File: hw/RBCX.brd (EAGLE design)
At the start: 100 x 100 mm, 470 parts, among them IC1 AMS1117-3.3, IC10 INA180A4, IC11 INA180A4, IC12 MPU-6050, IC13 STM32F103VCT6, IC2 DRV8833PWP, IC3 INA180A4, IC4 INA180A4, IC5 DRV8833PWP, IC6 INA180A4, IC7 INA180A4, IC8 INA180A4, IC9 INA180A4, P1 M1, P2 M2, P3 M3, P4 M4, Q1 NCE20P45Q, Q10 2N7002, Q2 NCE20P45Q, Q3 2N7002, Q4 2N7002, Q5 2N7002, Q6 2N7002, Q7 2N7002, Q8 2N7002, Q9 2N7002, X1 POWER_IN, X2 POWER_OUT, X3 52559-3092, X4 uUSB, Y1 5032/2P, Y2 3215_2P

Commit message: hw: jumpers modified to match 0603 resistors
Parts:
- removed R119, R126, R24, R25, R26, R47, R58: 0R, rcl_upravena:R0603
- SJ1, SJ2, SJ3, SJ4, SJ5, SJ8, SJ9: device jumper:SJ_2 -> jumper:SJ_2_DEFAULT
- SJ6, SJ7: device jumper:SJ_2 -> jumper:SJ_2_0603
- turned SJ1 to 270 degrees
- turned SJ2 to 270 degrees
- turned SJ4 to 0 degrees
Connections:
- net +3V3: now also SJ1.3, SJ2.3; no longer R26.1, R58.1, SJ1.1, SJ2.1
- net +3V3S: now also SJ4.3; no longer R119.1, R126.1, SJ4.1
- net +5V: now also SJ1.1, SJ2.1, SJ4.1; no longer R24.2, R25.2, R47.2, SJ1.3, SJ2.3, SJ4.3
- net ENC12_PWR: no longer R119.2
- net ENC34_PWR: no longer R126.2
- net ESP-I2C-PWR: no longer R25.1
- net ESP_SPI_PWR: no longer R24.1
- net ESP_UCOM_PWR: no longer R58.2
- net ESP_USART_PWR: no longer R26.2
- net STM_UART_PWR: no longer R47.1
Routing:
- net +5V: track 77.6 -> 71.2 mm

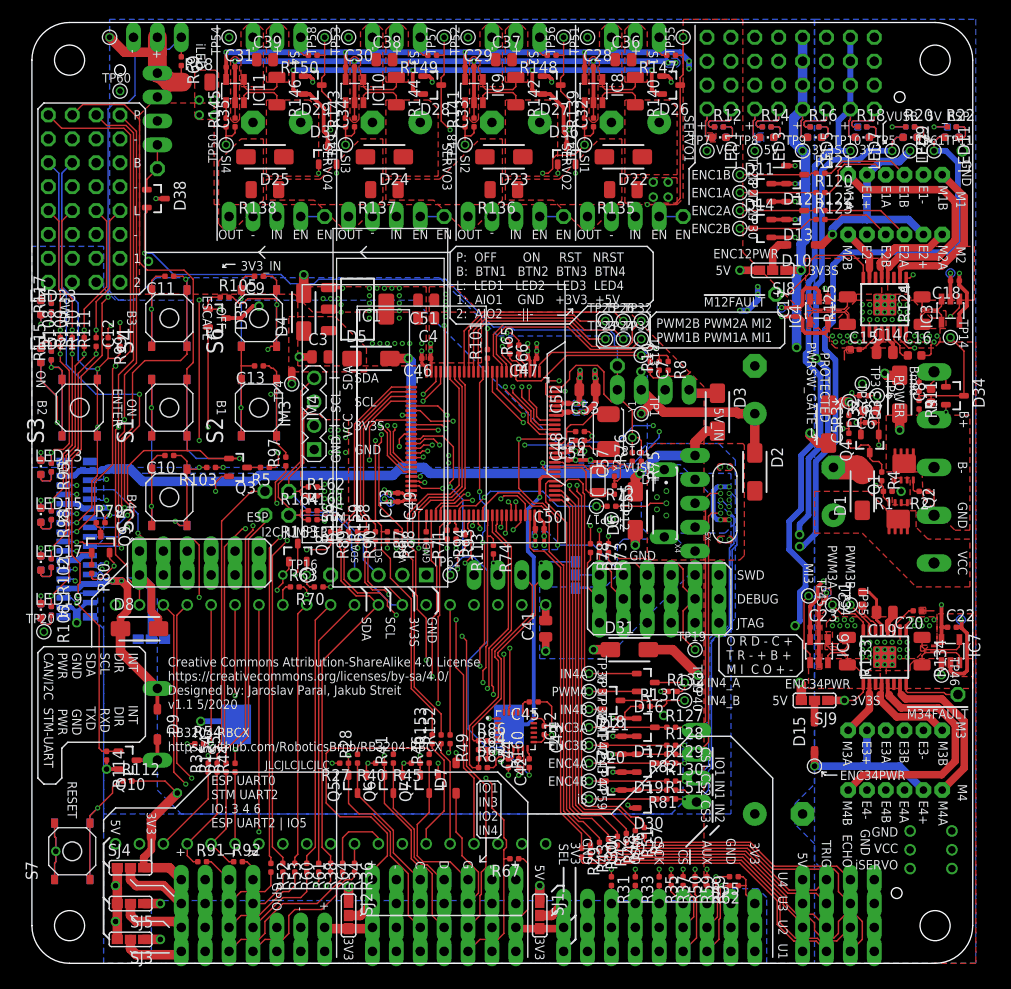
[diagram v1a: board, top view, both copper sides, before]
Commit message: hw: renumber parts
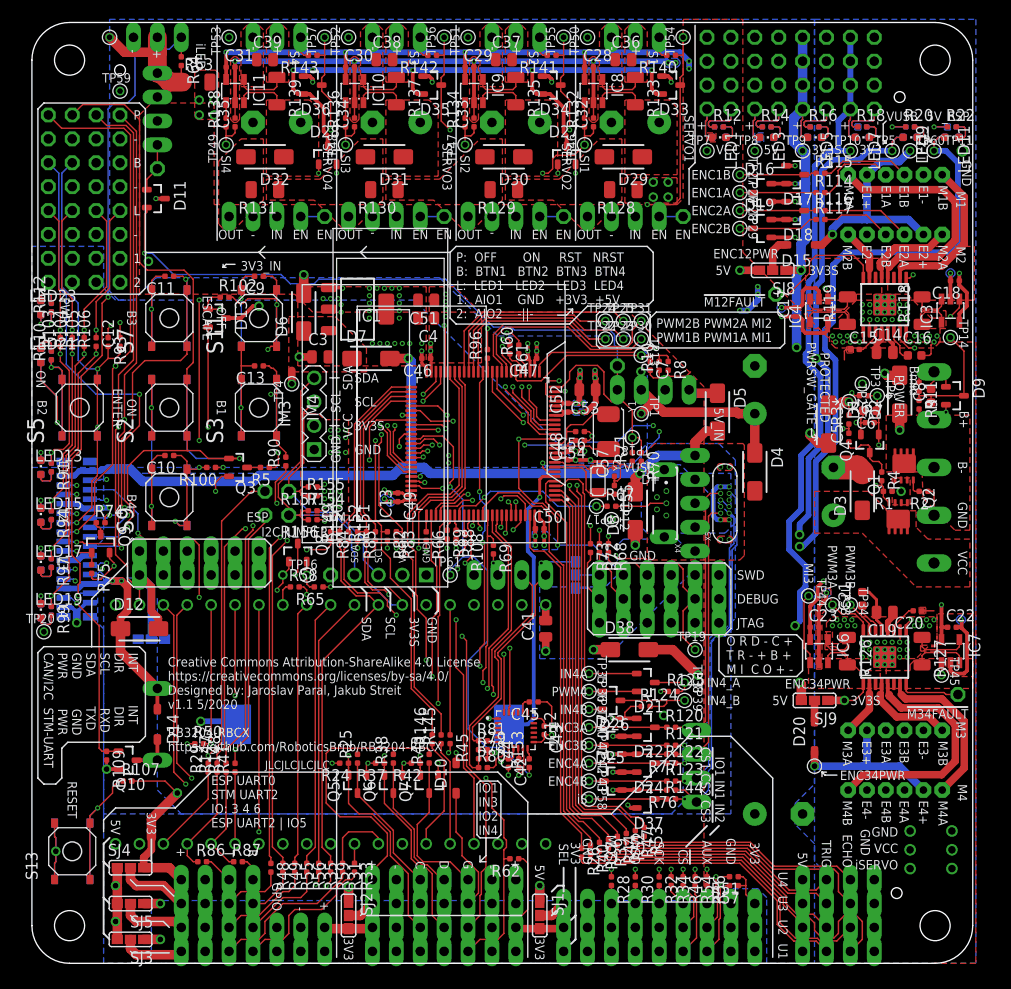
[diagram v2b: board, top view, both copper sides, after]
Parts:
- removed R158, R159, R160, R163, R164: 330R, rcl_upravena:R0402
- removed R161, R162: 4k7, rcl_upravena:R0402
- removed TP62: (no value), test_points:TP_06
- added R119, R126: 5m, rcl_upravena:R1206
- added R24, R25: 4k7, rcl_upravena:R0402
- added R26, R47, R58: 330R, rcl_upravena:R0402
- added TP21: (no value), test_points:TP_06
- D11, D13, D26, D27, D28: value BAS40-04 -> BAS40-05
- D12, D29, D30: value BAS40-04 -> SS34; device diode:SOT23 -> diode:SMA
- D14, D20: value BAS40-04 -> B5819W; device diode:SOT23 -> diode:SOD123
- D16, D35, D36, D37: value BAS40-05 -> BAS40-04
- D22, D23, D24, D25, D33: value SS34 -> BAS40-04; device diode:SMA -> diode:SOT23
- D38: value BAS40-05 -> SS34; device diode:SOT23 -> diode:SMA
- D7: value B5819W -> SS34; device diode:SOD123 -> diode:SMA
- D9: value B5819W -> BAS40-04; device diode:SOD123 -> diode:SOT23
- JP10: value ESP_UART -> ESP_I2C_AUX1_VSEL; device pinhead:1X04 -> pinhead:1X03
- JP11: value ESP_I2C_AUX1_VSEL -> ESP_UART_AUX
- JP12: value ESP_UART_AUX -> ESP_SPI_AUX1
- JP13: value ESP_SPI_AUX1 -> UTS2; device pinhead:1X03 -> pinhead:1X04
- JP14: value UTS2 -> ESP_I2C2_VSEL
- JP15: value ESP_I2C2_VSEL -> ESP_SPI2; device pinhead:1X04 -> pinhead:1X06
- JP16: value ESP_SPI2 -> UTS3; device pinhead:1X06 -> pinhead:1X04
- JP17: value UTS3 -> ESP_I2C_AUX2_VSEL; device pinhead:1X04 -> pinhead:1X03
- JP18: value ESP_I2C_AUX2_VSEL -> STM_UART; device pinhead:1X03 -> pinhead:1X04
- JP19: value STM_UART -> ESP_SPI_AUX2; device pinhead:1X04 -> pinhead:1X03
- JP20: value ESP_SPI_AUX2 -> UTS4; device pinhead:1X03 -> pinhead:1X04
- JP21: value UTS4 -> ESP_SPI3; device pinhead:1X04 -> pinhead:1X06
- JP22: value ESP_SPI3 -> ESP_I2C1; device pinhead:1X06 -> pinhead:1X04
- JP23: value ESP_I2C1 -> ESP_UCOM
- JP24: value ESP_UCOM -> ESP_SPI_AUX3; device pinhead:1X04 -> pinhead:1X03
- JP25: value ESP_SPI_AUX3 -> ESP_I2C_AUX1
- JP26: value ESP_I2C_AUX1 -> ESP_UCOM_AUX
- JP27: value ESP_UCOM_AUX -> ILED_EN; device pinhead:1X03 -> pinhead:1X01
- JP29: value ILED_EN -> AIO; device pinhead:1X01 -> pinhead:2X04
- JP30: value AIO -> ESP_I2C_AUX2; device pinhead:2X04 -> pinhead:1X03
- JP31: value ESP_I2C_AUX2 -> ILED
- JP32: value ILED -> USB; device pinhead:1X03 -> pinhead:1X05
- JP33: value USB -> SWD; device pinhead:1X05 -> pinhead:1X06
- JP34: value SWD -> DEBUG; device pinhead:1X06 -> pinhead:1X04
- JP35: value DEBUG -> USBC_AUX
- JP4: value BUZZER -> +5V; device pinhead:1X01 -> pinhead:2X04
- JP42: value BUTTONS -> LEDS
- JP43: value LEDS -> BUTTONS
- JP44: value PWR_BUTTONS -> BUZZER; device pinhead:2X04 -> pinhead:1X01
- JP45: value M12FAULT -> PWR_BUTTONS; device pinhead:1X01 -> pinhead:2X04
- JP46: value M34FAULT -> M12FAULT
- JP47: value SERVO1_EN -> M34FAULT
- JP48: value SERVO2_EN -> SERVO1_EN
- JP49: value SERVO3_EN -> SERVO2_EN
- JP5: value +5V -> VCC
- JP50: value SERVO4_EN -> SERVO3_EN
- JP51: value SERVO1 -> SERVO4_EN; device pinhead:1X03 -> pinhead:1X01
- JP52: value SERVO2 -> SERVO1
- JP53: value SERVO3 -> SERVO2
- JP54: value SERVO4 -> SERVO3
- JP55: value INTELIGENT_SERVO1 -> SERVO4; device iServo_connector:292161-3 -> pinhead:1X03
- JP56: value INTELIGENT_SERVO2 -> INTELIGENT_SERVO1
- JP57: value I2C_INTERCONNECT -> INTELIGENT_SERVO2; device pinhead:2X02 -> iServo_connector:292161-3
- JP58: value USBC_AUX -> I2C_INTERCONNECT; device pinhead:1X04 -> pinhead:2X02
- JP6: value VCC -> UTS1; device pinhead:2X04 -> pinhead:1X04
- JP7: value UTS1 -> ESP_I2C1_VSEL
- JP8: value ESP_I2C1_VSEL -> ESP_SPI1; device pinhead:1X04 -> pinhead:1X06
- JP9: value ESP_SPI1 -> ESP_UART; device pinhead:1X06 -> pinhead:1X04
- R102: value 330R -> 2k2
- R105, R147, R148, R149, R150, R151: value 2k2 -> 330R
- R107, R109: value 330R -> 1M
- R110, R111, R154, R155, R37, R38, R42, R43, R50, R64, R78: value 330R -> 4k7
- R112: value 1M -> 1k
- R113, R77: value 330R -> 1k
- R114: value 1M -> 2k2
- R115, R116: value 4k7 -> 2k2
- R117, R141, R143: value 1k -> 2k2
- R118, R139: value 1k -> 5m; device rcl_upravena:R0402 -> rcl_upravena:R1206
- R124, R125: value 5m -> 10k; device rcl_upravena:R1206 -> rcl_upravena:R0402
- R127: value 2k2 -> 5m; device rcl_upravena:R0402 -> rcl_upravena:R1206
- R128, R129, R130: value 2k2 -> 0R; device rcl_upravena:R0402 -> rcl_upravena:R1206
- R131: value 10k -> 0R; device rcl_upravena:R0402 -> rcl_upravena:R1206
- R132, R76: value 10k -> 1k
- R134: value 5m -> 1k; device rcl_upravena:R1206 -> rcl_upravena:R0402
- R135, R137: value 0R -> 5m
- R136, R138: value 0R -> 1k; device rcl_upravena:R1206 -> rcl_upravena:R0402
- R140, R142, R144: value 5m -> 2k2; device rcl_upravena:R1206 -> rcl_upravena:R0402
- R145, R81, R82: value 1k -> 330R
- R146: value 5m -> 330R; device rcl_upravena:R1206 -> rcl_upravena:R0402
- R27, R28, R40, R41, R45, R46, R54, R69, R83, R84: value 4k7 -> 330R
- R51, R57, R74: value 330R -> 100k
- R55, R80: value 100k -> 330R
- R62, R79: value 100k -> 4k7
- R63: value 330R -> 0R; device rcl_upravena:R0402 -> rcl_upravena:R1206
- R67: value 4k7 -> 1k5
- R68: value 0R -> 330R; device rcl_upravena:R1206 -> rcl_upravena:R0402
- R70: value 330R -> 5k6
- R71: value 330R -> 10k
- R72: value 1k5 -> 330R
- R75: value 5k6 -> 100k
- moved JP55 109.5 mm to (26.0, 98.4), turned to 0 degrees
- moved JP31 103.5 mm to (13.3, 98.4), turned to 0 degrees
- moved R114 96.6 mm to (83.8, 81.9), turned to 0 degrees
- moved JP6 94.2 mm to (85.7, 1.27), turned to 180 degrees
- moved R118 92.6 mm to (94.6, 69.4), flipped to the top
- moved D9 91.7 mm to (98.1, 60.3), turned to 180 degrees
- moved TP59 90.3 mm to (9.37, 92.7), turned to 0 degrees
- moved R147 89.8 mm to (19.7, 20.8), turned to 90 degrees
- moved R64 87.2 mm to (15.9, 95.9)
- moved TP60 86.8 mm to (95.9, 86.4)
- moved TP58 85.7 mm to (59.2, 17.5), turned to 270 degrees
- moved D12 84.8 mm to (11.4, 35.6), turned to 0 degrees
- moved JP30 84.4 mm to (48.9, 1.27)
- moved R115 84.0 mm to (83.8, 84.0), turned to 0 degrees
- moved R148 83.3 mm to (20.6, 20.8), turned to 90 degrees
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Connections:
- net !M12_FAULT: now also JP46.1; no longer JP45.1
- net !M34_FAULT: now also JP47.1; no longer JP46.1
- net +3V3: now also JP11.3, JP15.1, JP19.3, JP21.1, JP24.3, JP30.3, R24.2, R37.2, R42.2, R50.1, R51.1, R57.1; no longer JP13.3, JP16.1, JP20.3, JP23.1, JP27.3, JP31.3, R27.2, R40.2, R45.2, R54.1, R55.1, R67.1
- net +3V3S: now also D11.3, D13.3, D16.2, D22.2, D23.2, D24.2, D25.2, D27.3, D28.3, D33.2, D35.2, D36.2, D37.2, D9.2, JP29.5, JP29.6, JP33.1, R107.2, R154.2, R155.2, R78.2, R79.2; no longer D11.2, D12.2, D13.2, D14.2, D20.2, D26.2, D27.2, D28.2, D29.2, D30.2, D35.3, D36.3, D37.3, D38.3, JP30.5, JP30.6, JP35.1, R112.2, R161.2, R162.2, R83.2, R84.2
- net +5V: now also D1.A, D12.C, D14.C, D38.A, D5.C, D6.A, JP13.1, JP16.1, JP20.1, JP29.7, JP29.8, JP4.1, JP4.3, JP4.5, JP4.7, JP6.1, R128.1, R63.2; no longer D3.C, D31.A, D32.A, D4.A, D8.C, D9.C, JP14.1, JP17.1, JP21.1, JP30.7, JP30.8, JP5.1, JP5.3, JP5.5, JP5.7, JP7.1, R135.1, R68.2
- net 3V3_EN: now also D11.2; no longer D38.2
- net 3V3_IN: now also D6.C, D7.C; no longer D4.C, D5.C
- net 5V_IN: now also D4.C; no longer D2.C
- net BAT+_PROTECTED: now also D1.C, D2.C; no longer D32.C, D33.C
- net BOOT0: now also R75.1; no longer R80.1
- net BOOT1_PULL-DOWN: now also R74.1; no longer R79.1
- net BUTTON-1: now also JP43.1, R90.2, S3.C, S3.D, S4.C, S4.D; no longer JP42.1, R97.2, S2.C, S2.D, S8.C, S8.D
- net BUTTON-2: now also JP43.3, R93.2, S5.C, S5.D, S6.C, S6.D; no longer JP42.3, R99.2, S3.C, S3.D, S9.C, S9.D
- net BUTTON-3: now also JP43.5, R74.2, R96.2, S7.C, S7.D, S8.C, S8.D; no longer JP42.5, R101.2, R79.2, S10.C, S10.D, S4.C, S4.D
- net BUTTON-4: now also JP43.7, R100.2, S10.C, S10.D, S9.C, S9.D; no longer JP42.7, R103.2, S11.C, S11.D, S5.C, S5.D
- net BUTTON-OFF: now also JP45.1, R102.2, S11.C, S11.D; no longer JP44.1, R105.2, S6.C, S6.D
- net BUTTON-ON: now also JP45.3, S2.C, S2.D; no longer JP44.3, S14.C, S14.D
- net BUTTON1: now also R90.1; no longer R97.1
- net BUTTON2: now also R93.1; no longer R99.1
- net BUTTON3: now also R96.1; no longer R101.1
- net BUTTON4: now also R100.1; no longer R103.1
- net BUTTON_OFF: now also D13.1, R102.1; no longer D35.1, R105.1
- net BUZZER: now also R108.1; no longer R113.1
- net BUZZER-: now also D14.A; no longer D9.A
- net BUZZER-GATE: now also JP44.1, R108.2, R109.1; no longer JP4.1, R113.2, R114.1
- net CONTROL-DIR: now also R84.2; no longer R89.2
- net CONTROL-INT: now also R85.2; no longer R90.2
- net CONTROL-RX/SDA: now also R83.2; no longer R88.2
- net CONTROL-TX/SCL: now also R82.2; no longer R87.2
- net CONTROL_RX/SDA: now also R145.2, R83.1; no longer R152.2, R88.1
- net CONTROL_TX/SCL: now also R146.2, R82.1; no longer R153.2, R87.1
- net DEBUG-RX: now also JP34.3, R72.2; no longer JP35.3, R77.2
- net DEBUG-TX: now also JP34.4, R73.2; no longer JP35.4, R78.2
- net DEBUG_RX: now also R72.1; no longer R77.1
- net DEBUG_TX: now also R73.1; no longer R78.1
- net ENC12PWR: now also D15.C, TP21.P$1; no longer D10.C, TP22.P$1
- net ENC12_PWR: now also D15.A; no longer D10.A
- net ENC1A: now also D16.3, R114.1, TP26.P$1; no longer D11.3, R120.1, TP27.P$1
- net ENC1B: now also D17.3, R115.1, TP27.P$1; no longer D12.3, R121.1, TP28.P$1
- net ENC2A: now also D18.3, R116.1, TP28.P$1; no longer D13.3, R122.1, TP29.P$1
- net ENC2B: now also D19.3, R117.1, TP29.P$1; no longer D14.3, R123.1, TP30.P$1
- net ENC34PWR: now also D20.C, TP32.P$1; no longer D15.C, TP33.P$1
- net ENC34_PWR: now also D20.A; no longer D15.A
- net ENC3A: now also D22.3, R120.1, TP40.P$1; no longer D17.3, R127.1, TP41.P$1
- net ENC3B-SWO: now also R69.2; no longer R74.2
- net ENC3B/SWO: now also D23.3, R121.1, R69.1, TP41.P$1; no longer D18.3, R128.1, R74.1, TP42.P$1
- net ENC4A: now also D24.3, R122.1, TP42.P$1; no longer D19.3, R129.1, TP43.P$1
- net ENC4B: now also D25.3, R123.1, TP43.P$1; no longer D20.3, R130.1, TP44.P$1
- net ENC_1A: now also R114.2; no longer R120.2
- net ENC_1B: now also R115.2; no longer R121.2
- net ENC_2A: now also R116.2; no longer R122.2
- net ENC_2B: now also R117.2; no longer R123.2
- net ENC_3A: now also R120.2; no longer R127.2
- net ENC_3B: now also R121.2; no longer R128.2
- net ENC_4A: now also R122.2; no longer R129.2
- net ENC_4B: now also R123.2; no longer R130.2
- net ESP-I2C-PWR: now also JP10.3, JP14.1, JP17.3, JP7.1, R25.2, R38.2, R43.2; no longer JP11.3, JP15.1, JP18.3, JP8.1, R28.2, R41.2, R46.2
- net ESP-I2C-SCL: now also JP22.3, JP58.3, R24.1, R29.2; no longer JP23.3, JP57.3, R27.1, R32.2
- net ESP-I2C-SCL-VSEL: now also JP14.3, JP7.3, R25.1; no longer JP15.3, JP8.3, R28.1
- net ESP-I2C-SDA: now also JP22.4, JP58.1, R37.1, R41.2; no longer JP23.4, JP57.1, R40.1, R44.2
- net ESP-I2C-SDA-VSEL: now also JP14.4, JP7.4, R38.1; no longer JP15.4, JP8.4, R41.1
- net ESP-SPI-!CS1: now also JP8.6, R34.2; no longer JP9.6, R37.2
- net ESP-SPI-!CS2: now also JP15.6, R46.2; no longer JP16.6, R50.2
- net ESP-SPI-!CS3: now also JP21.6, R54.2; no longer JP22.6, R59.2
- net ESP-SPI-MISO: now also JP15.4, JP21.4, JP8.4, R30.2; no longer JP16.4, JP22.4, JP9.4, R33.2
- net ESP-SPI-MOSI: now also JP15.3, JP21.3, JP8.3, R28.2; no longer JP16.3, JP22.3, JP9.3, R31.2
- net ESP-SPI-SCK: now also JP15.5, JP21.5, JP8.5, R32.2; no longer JP16.5, JP22.5, JP9.5, R35.2
- net ESP-UART-RX: now also R87.2; no longer R92.2
- net ESP-UART-TX: now also R86.2; no longer R91.2
- net ESP-USART-RX: now also JP9.3, R31.2; no longer JP10.3, R34.2
- net ESP-USART-TX: now also JP9.4, R33.2; no longer JP10.4, R36.2
- net ESP_+5V: now also D38.C, D8.C, TP60.P$1; no longer D31.C, D6.C, TP61.P$1
- net ESP_EN: now also D13.2, JP45.5, R107.1, S14.C, S14.D, TP59.P$1; no longer D35.2, JP44.5, R112.1, S7.C, S7.D, TP60.P$1
- net ESP_SPI_PWR: now also JP8.1; no longer JP9.1
- net ESP_UCOM_PWR: now also JP23.1; no longer JP24.1
- net ESP_USART_PWR: now also JP9.1; no longer JP10.1
- net EXPANDER_COM_PWR: now also D12.A; no longer D8.A
- net EXPANDER_RX: now also R146.1; no longer R153.1
- net EXPANDER_TX: now also R145.1; no longer R152.1
- net GND: now also D16.1, D22.1, D23.1, D24.1, D25.1, D3.A, D33.1, D35.1, D36.1, D37.1, D9.1, JP13.4, JP14.2, JP16.4, JP17.2, JP20.4, JP21.2, JP29.3, JP29.4, JP30.2, JP31.3, JP32.5, JP33.3, JP34.2, JP4.2, JP4.4, JP4.6, JP4.8, JP45.2, JP45.4, JP45.6, JP45.8, JP57.3, JP7.2, R109.2, R110.1, R111.1, R112.1, R113.1, R119.1, R126.1, R127.1, R71.1, R75.2, R76.2, R77.2; no longer D1.A, D11.1, D12.1, D13.1, D14.1, D20.1, D26.1, D27.1, D28.1, D29.1, D30.1, JP13.2, JP14.4, JP16.2, JP17.4, JP20.2, JP21.4, JP27.2, JP30.3, JP30.4, JP31.2, JP32.3, JP33.5, JP34.3, JP35.2, JP44.2, JP44.4, JP44.6, JP44.8, JP51.3, JP6.2, JP6.6, JP6.8, JP7.4, R114.2, R115.1, R116.1, R117.1, R131.1, R132.1, R133.1, R134.1, R76.1, R80.2, R81.2, R82.2
- net GPIO-1: now also JP12.1, R36.2; no longer JP13.1, R39.2
- net GPIO-1-VSEL: now also JP10.1, R43.1; no longer JP11.1, R46.1
- net GPIO-2: now also JP25.1, R58.2; no longer JP26.1, R63.2
- net GPIO-3: now also JP23.3, R55.2; no longer JP24.3, R60.2
- net GPIO-4: now also JP23.4, R56.2; no longer JP24.4, R61.2
- net GPIO-5: now also JP11.1, R35.2; no longer JP12.1, R38.2
- net GPIO-6: now also JP26.1, R59.2; no longer JP27.1, R64.2
- net GPIO-7: now also R42.1, R45.2; no longer R45.1, R49.2
- net GPIO1: now also R36.1; no longer R39.1
- net GPIO2: now also R58.1; no longer R63.1
- net GPIO3: now also R55.1; no longer R60.1
- net GPIO4: now also R56.1; no longer R61.1
- net GPIO5: now also R35.1; no longer R38.1
- net GPIO6/TMS: now also R149.1, R59.1; no longer R156.1, R64.1
- net GPIO7/TCK: now also R150.1, R45.1; no longer R157.1, R49.1
- net I2C_SCL: now also R29.1; no longer R32.1
- net I2C_SDA: now also R41.1; no longer R44.1
- net ILED: now also R65.2; no longer R70.2
- net ILED-5V: now also JP31.1, R64.1; no longer JP32.1, R69.1
- net ILED_EN: now also D11.1, JP27.1; no longer D38.1, JP29.1
- net ILED_PWR: now also JP31.2, R63.1, R64.2; no longer JP32.2, R68.1, R69.2
- net IN1: now also JP19.1, R51.2; no longer JP20.1, R55.2
- net IN2: now also JP24.1, R57.2; no longer JP25.1, R62.2
- net IN3: now also D10.A, R50.2; no longer D7.A, R54.2
- net IN3-5V: now also D10.C, JP17.1; no longer D7.C, JP18.1
- net IN4: now also JP30.1, R62.2; no longer JP31.1, R67.2
- net IN4A: now also D21.1, TP35.P$1; no longer D16.1, TP36.P$1
- net IN4B: now also D26.2, TP37.P$1; no longer D21.2, TP38.P$1
- net IN4_A: now also D21.3, R125.2, TP38.P$1; no longer D16.3, R132.2, TP39.P$1
- net IN4_B: now also D26.3, R124.2, TP39.P$1; no longer D21.3, R131.2, TP40.P$1
- net INTELLIGENT_SERVO: now also D37.3, R144.1, TP58.P$1; no longer D30.3, R151.1, TP59.P$1
- net ISERVO: now also JP57.1, R144.2; no longer JP55.1, R151.2
- net I_LED/TDI: now also R151.1, R65.1; no longer R158.1, R70.1
- net LED-1: now also JP42.1, R103.2; no longer JP43.1, R108.2
- net LED-2: now also JP42.3, R104.2; no longer JP43.3, R109.2
- net LED-3: now also JP42.5, R105.2; no longer JP43.5, R110.2
- net LED-4: now also JP42.7, R106.2; no longer JP43.7, R111.2
- net LED1: now also R103.1, R91.1, R92.1; no longer R108.1, R95.1, R96.1
- net LED2: now also R104.1, R94.1, R95.1; no longer R100.1, R109.1, R98.1
- net LED3: now also R105.1, R97.1, R98.1; no longer R102.1, R104.1, R110.1
- net LED4: now also R101.1, R99.1; no longer R107.1, R111.1
- net LED_1: now also R91.2; no longer R95.2
- net LED_1B: now also R92.2; no longer R96.2
- net LED_2: now also R94.2; no longer R98.2
- net LED_2B: now also R95.2; no longer R100.2
- net LED_3: now also R97.2; no longer R102.2
- net LED_3B: now also R98.2; no longer R104.2
- net LED_4: now also R99.2; no longer R106.2
- net LED_4B: now also R101.2; no longer R107.2
- net M1GND: now also R118.2; no longer R124.2
- net M2GND: now also R119.2; no longer R125.2
- net M3GND: now also R126.2; no longer R133.2
- net M4GND: now also R127.2; no longer R134.2
- net MI1: now also TP30.P$1; no longer TP31.P$1
- net MI2: now also TP31.P$1; no longer TP32.P$1
- net MI3: now also TP44.P$1; no longer TP45.P$1
- net MI4: now also TP45.P$1; no longer TP46.P$1
- net MPU-INT: now also R153.2; no longer R160.2
- net MPU-SCL: now also R78.1, R80.1; no longer R83.1, R85.1
- net MPU-SDA: now also R79.1, R81.1; no longer R84.1, R86.1
- net MPU_INT: now also R153.1, TP61.P$1; no longer R160.1, TP62.P$1
- net MPU_SCL: now also R80.2; no longer R85.2
- net MPU_SDA: now also R81.2; no longer R86.2
- net NRST: now also JP33.5, JP45.7; no longer JP34.5, JP44.7
- net PWM1A: now also TP23.P$1; no longer TP24.P$1
- net PWM1B: now also TP22.P$1; no longer TP23.P$1
- net PWM2A: now also TP25.P$1; no longer TP26.P$1
- net PWM2B: now also TP24.P$1; no longer TP25.P$1
- net PWM3A: now also TP33.P$1; no longer TP34.P$1
- net PWM3B: now also TP34.P$1; no longer TP35.P$1
- net PWM4: now also D21.2, D26.1, TP36.P$1; no longer D16.2, D21.1, TP37.P$1
- net PWRLED_+3V3S1: now also R112.2; no longer R117.2
- net PWRLED_+3V3S_B1: now also R113.2; no longer R118.2
- net PWRLED_VCC1: now also R110.2; no longer R115.2
- net PWRLED_VCC_B1: now also R111.2; no longer R116.2
- net SERVO1: now also D33.3, R140.1, TP54.P$1; no longer D26.3, R147.1, TP55.P$1
- net SERVO1PWR: now also D29.A, R128.2, R129.1; no longer D22.A, R135.2, R136.1
- net SERVO1_EN: now also D27.2, JP48.1; no longer D36.2, JP47.1
- net SERVO1_PWR: now also D29.C, R133.2; no longer D22.C, R140.2
- net SERVO2: now also D34.3, R141.1, TP55.P$1; no longer D27.3, R148.1, TP56.P$1
- net SERVO2PWR: now also D30.A, R129.2, R130.1; no longer D23.A, R136.2, R137.1
- net SERVO2_EN: now also D27.1, JP49.1; no longer D36.1, JP48.1
- net SERVO2_PWR: now also D30.C, R135.2; no longer D23.C, R142.2
- net SERVO3: now also D35.3, R142.1, TP56.P$1; no longer D28.3, R149.1, TP57.P$1
- net SERVO3PWR: now also D31.A, R130.2, R131.1; no longer D24.A, R137.2, R138.1
- net SERVO3_EN: now also D28.2, JP50.1; no longer D37.2, JP49.1
- net SERVO3_PWR: now also D31.C, R137.2; no longer D24.C, R144.2
- net SERVO4: now also D36.3, R143.1, TP57.P$1; no longer D29.3, R150.1, TP58.P$1
- net SERVO4PWR: now also D32.A, R131.2; no longer D25.A, R138.2
- net SERVO4_EN: now also D28.1, JP51.1; no longer D37.1, JP50.1
- net SERVO4_PWR: now also D32.C, R139.2; no longer D25.C, R146.2
- net SERVO_1: now also JP52.1, R140.2; no longer JP51.1, R147.2
- net SERVO_1_PWR: now also JP52.2, R133.1, TP50.P$1; no longer JP51.2, R140.1, TP51.P$1
- net SERVO_2: now also JP53.1, R141.2; no longer JP52.1, R148.2
- net SERVO_2_PWR: now also JP53.2, R135.1, TP51.P$1; no longer JP52.2, R142.1, TP52.P$1
- net SERVO_3: now also JP54.1, R142.2; no longer JP53.1, R149.2
- net SERVO_3_PWR: now also JP54.2, R137.1, TP52.P$1; no longer JP53.2, R144.1, TP53.P$1
- net SERVO_4: now also JP55.1, R143.2; no longer JP54.1, R150.2
- net SERVO_4_PWR: now also JP55.2, R139.1, TP53.P$1; no longer JP54.2, R146.1, TP54.P$1
- net SI1: now also R132.1, TP46.P$1; no longer R139.1, TP47.P$1
- net SI2: now also R134.1, TP47.P$1; no longer R141.1, TP48.P$1
- net SI3: now also R136.1, TP48.P$1; no longer R143.1, TP49.P$1
- net SI4: now also R138.1, TP49.P$1; no longer R145.1, TP50.P$1
- net SI_1: now also R132.2; no longer R139.2
- net SI_2: now also R134.2; no longer R141.2
- net SI_3: now also R136.2; no longer R143.2
- net SI_4: now also R138.2; no longer R145.2
- net SPI_!SS1: now also R34.1; no longer R37.1
- net SPI_!SS2: now also R46.1; no longer R50.1
- net SPI_!SS3!/TDO: now also R152.1, R54.1; no longer R159.1, R59.1
- net SPI_MISO: now also R30.1; no longer R33.1
- net SPI_MOSI: now also R28.1; no longer R31.1
- net SPI_SCK: now also R32.1; no longer R35.1
- net STM-AIO1: now also JP29.1, R60.2; no longer JP30.1, R65.2
- net STM-AIO2: now also JP29.2, R61.1; no longer JP30.2, R66.1
- net STM-CAN-RX: now also R89.2; no longer R94.2
- net STM-CAN-TX: now also R88.2; no longer R93.2
- net STM-I2C-SCL: now also JP58.4, R155.1, R157.2; no longer JP57.4, R162.1, R164.2
- net STM-I2C-SDA: now also JP58.2, R154.1, R156.2; no longer JP57.2, R161.1, R163.2
- net STM-UART-RX: now also JP18.4, R49.2; no longer JP19.4, R53.2
- net STM-UART-TX: now also JP18.3, R48.2; no longer JP19.3, R52.2
- net STM_AIO1: now also R60.1; no longer R65.1
- net STM_AIO2: now also R61.2; no longer R66.2
- net STM_CAN_RX: now also R89.1; no longer R94.1
- net STM_CAN_TX: now also R88.1; no longer R93.1
- net STM_I2C_SCL: now also R157.1; no longer R164.1
- net STM_I2C_SDA: now also R156.1; no longer R163.1
- net STM_SPI_!CS: now also R149.2, R84.1; no longer R156.2, R89.1
- net STM_SPI_MISO: now also R152.2, R85.1; no longer R159.2, R90.1
- net STM_SPI_MOSI: now also R151.2; no longer R158.2
- net STM_SPI_SCK: now also R150.2; no longer R157.2
- net STM_UART_PWR: now also JP18.1; no longer JP19.1
- net SWCLK: now also R66.1; no longer R71.1
- net SWCLK_: now also JP33.2, R66.2; no longer JP34.2, R71.2
- net SWDIO: now also R68.1; no longer R73.1
- net SWDIO_: now also JP33.4, R68.2; no longer JP34.4, R73.2
- net SWO: now also JP33.6; no longer JP34.6
- net TUNNEL_RX: now also R147.2; no longer R154.2
- net TUNNEL_TX: now also R148.2; no longer R155.2
- net UART2_RX: now also R31.1; no longer R34.1
- net UART2_TX: now also R33.1; no longer R36.1
- net UART_RX: now also R148.1, R87.1; no longer R155.1, R92.1
- net UART_TX: now also R147.1, R86.1; no longer R154.1, R91.1
- net USB_CC1: now also JP35.2, R77.1; no longer JP58.2, R82.1
- net USB_CC2: now also JP35.4, R76.1; no longer JP58.4, R81.1
- net USB_DM: now also JP32.2; no longer JP33.2
- net USB_DP: now also JP32.3, R67.2; no longer JP33.3, R72.2
- net USB_DP_PULLUP: now also R67.1; no longer R72.1
- net USB_ID: now also JP32.4; no longer JP33.4
- net USB_SBU1: now also JP35.1; no longer JP58.1
- net USB_SBU2: now also JP35.3; no longer JP58.3
- net USER_RX: now also R49.1; no longer R53.1
- net USER_TX: now also R48.1; no longer R52.1
- net UTS1-ECHO: now also JP6.3, R27.2; no longer JP7.3, R30.2
- net UTS1-TRIG: now also JP6.2, R26.2; no longer JP7.2, R29.2
- net UTS1_ECHO: now also R27.1; no longer R30.1
- net UTS1_TRIG: now also R26.1; no longer R29.1
- net UTS2-ECHO: now also JP13.3, R40.2; no longer JP14.3, R43.2
- net UTS2-TRIG: now also JP13.2, R39.2; no longer JP14.2, R42.2
- net UTS2_ECHO: now also R40.1; no longer R43.1
- net UTS2_TRIG: now also R39.1; no longer R42.1
- net UTS3-ECHO: now also JP16.3, R47.2; no longer JP17.3, R51.2
- net UTS3-TRIG: now also JP16.2, R44.2; no longer JP17.2, R48.2
- net UTS3_ECHO: now also R47.1; no longer R51.1
- net UTS3_TRIG: now also R44.1; no longer R48.1
- net UTS4-ECHO: now also JP20.3, R53.2; no longer JP21.3, R57.2
- net UTS4-TRIG: now also JP20.2, R52.2; no longer JP21.2, R56.2
- net UTS4_ECHO: now also R53.1; no longer R57.1
- net UTS4_TRIG: now also R52.1; no longer R56.1
- net VCC: now also D3.C, D4.A, JP5.1, JP5.3, JP5.5, JP5.7, JP57.2; no longer D1.C, D2.A, JP55.2, JP6.1, JP6.3, JP6.5, JP6.7
- net VUSB: now also D2.A, D7.A, D8.A, JP32.1, R70.2; no longer D3.A, D33.A, D6.A, JP33.1, R75.2
- net VUSB_DET: now also R70.1, R71.2; no longer R75.1, R76.2
- net V_BAT/2: now also D9.3; no longer D34.3

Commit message: hw: fix value of R74
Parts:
- R74: value 100k -> 330R
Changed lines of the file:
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@@
 <attribute name="VALUE" x="4.445" y="42.545" size="1.27" layer="27" rot="R270"/>
 </element>
-<element name="R74" library="rcl_upravena" package="R0402" value="100k" x="7.3025" y="46.83125" smashed="yes">
+<element name="R74" library="rcl_upravena" package="R0402" value="330R" x="7.3025" y="46.83125" smashed="yes">
 <attribute name="NAME" x="6.6675" y="47.46625" size="1.27" layer="25"/>
 <attribute name="VALUE" x="6.6675" y="44.92625" size="1.27" layer="27"/>

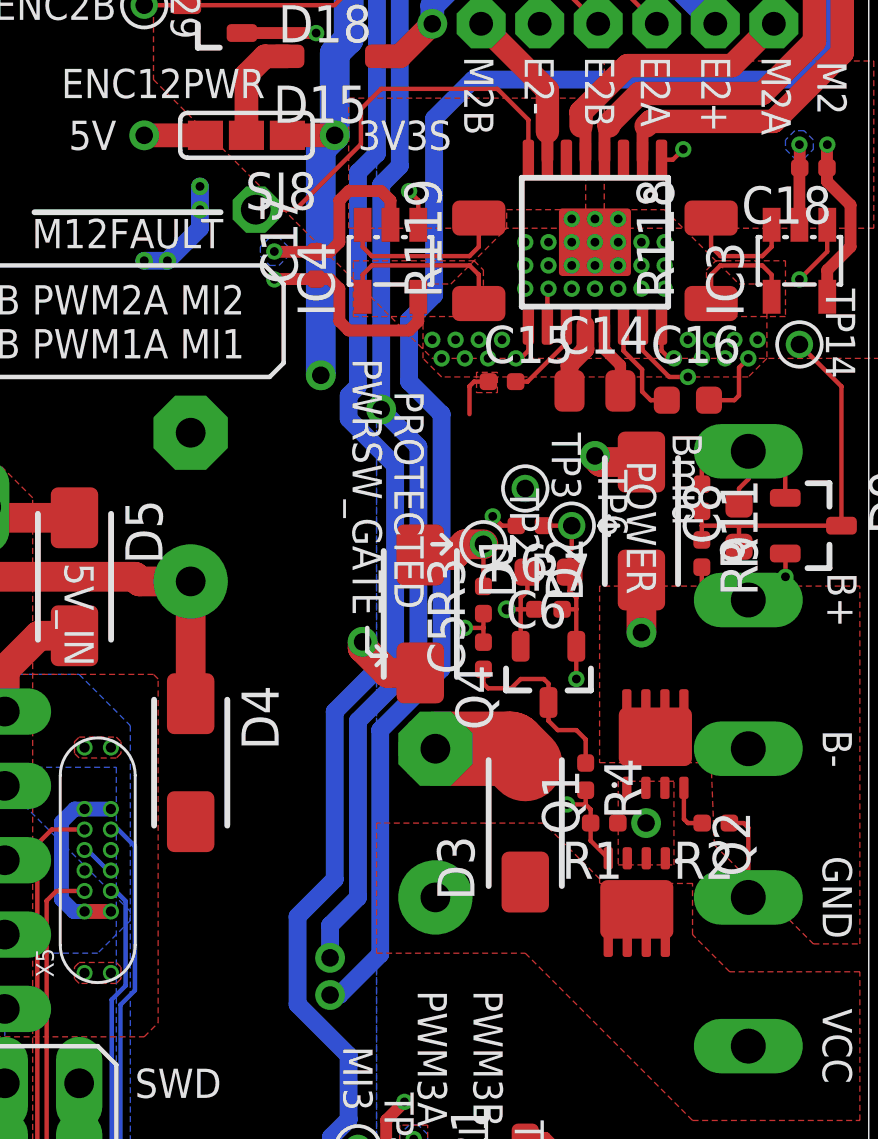
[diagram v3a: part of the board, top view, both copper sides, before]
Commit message: hw: replace D1 with smaller one (SS34 -> B5819W)
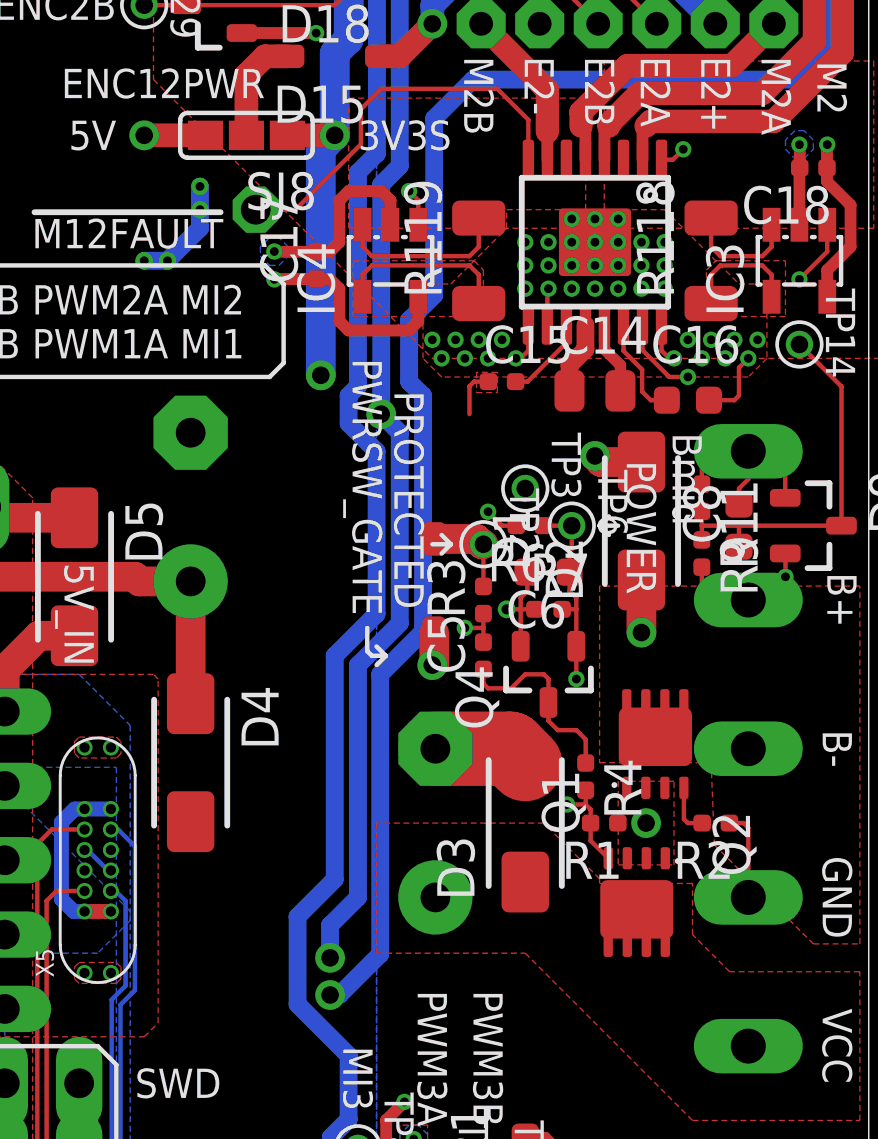
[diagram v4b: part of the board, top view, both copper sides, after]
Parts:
- D1: value SS34 -> B5819W; device diode:SMA -> diode:SOD123
- moved D1 1.06 mm to (85.2, 58.3)
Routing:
- net +5V: track 71.2 -> 87.2 mm
- net BUTTON-ON: track 156.5 -> 157.9 mm
- net POWER: track 47.1 -> 47.7 mm
- net VUSB: track 169.8 -> 169.3 mm
- net BAT+_PROTECTED: track 18.8 -> 18.2 mm
- net ESP_+5V: track 87.1 -> 86.6 mm
- net +3V3: track 122.4 -> 121.9 mm

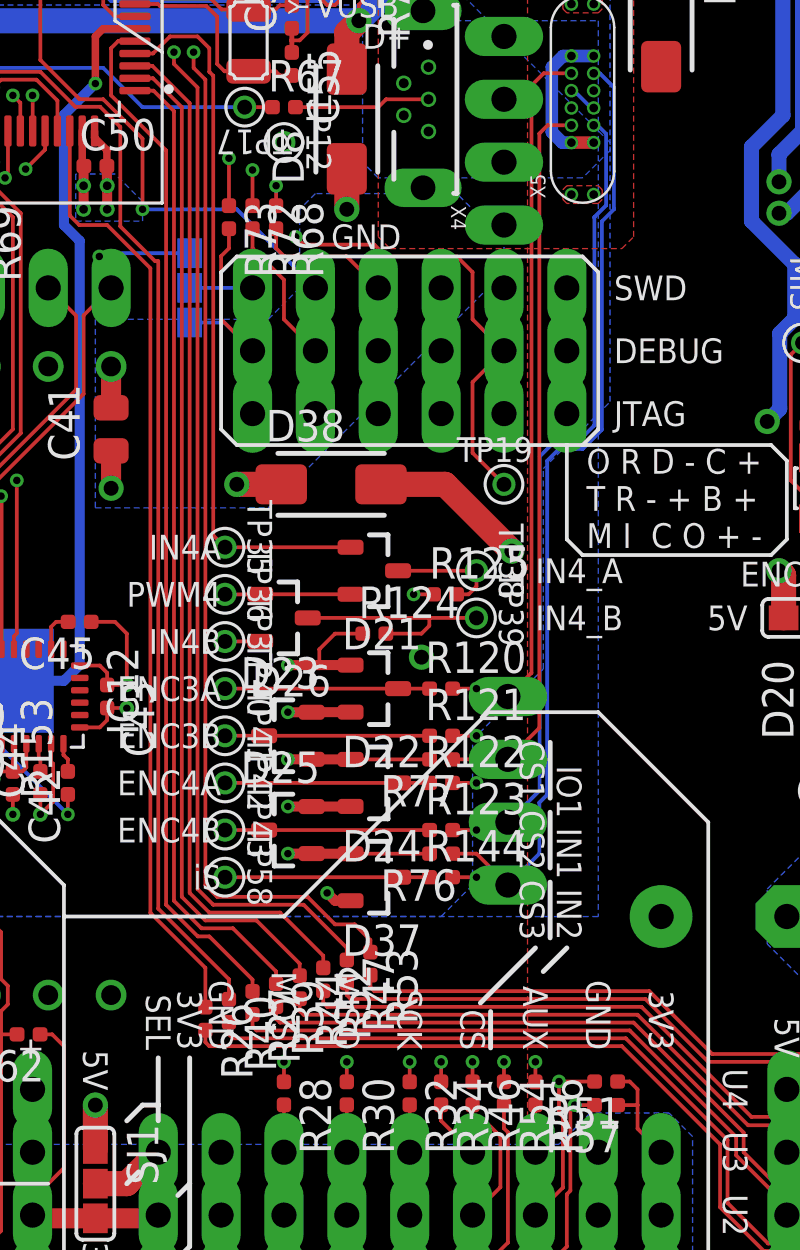
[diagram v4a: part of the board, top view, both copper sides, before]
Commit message: hw: move some resistors, because of silkscreen
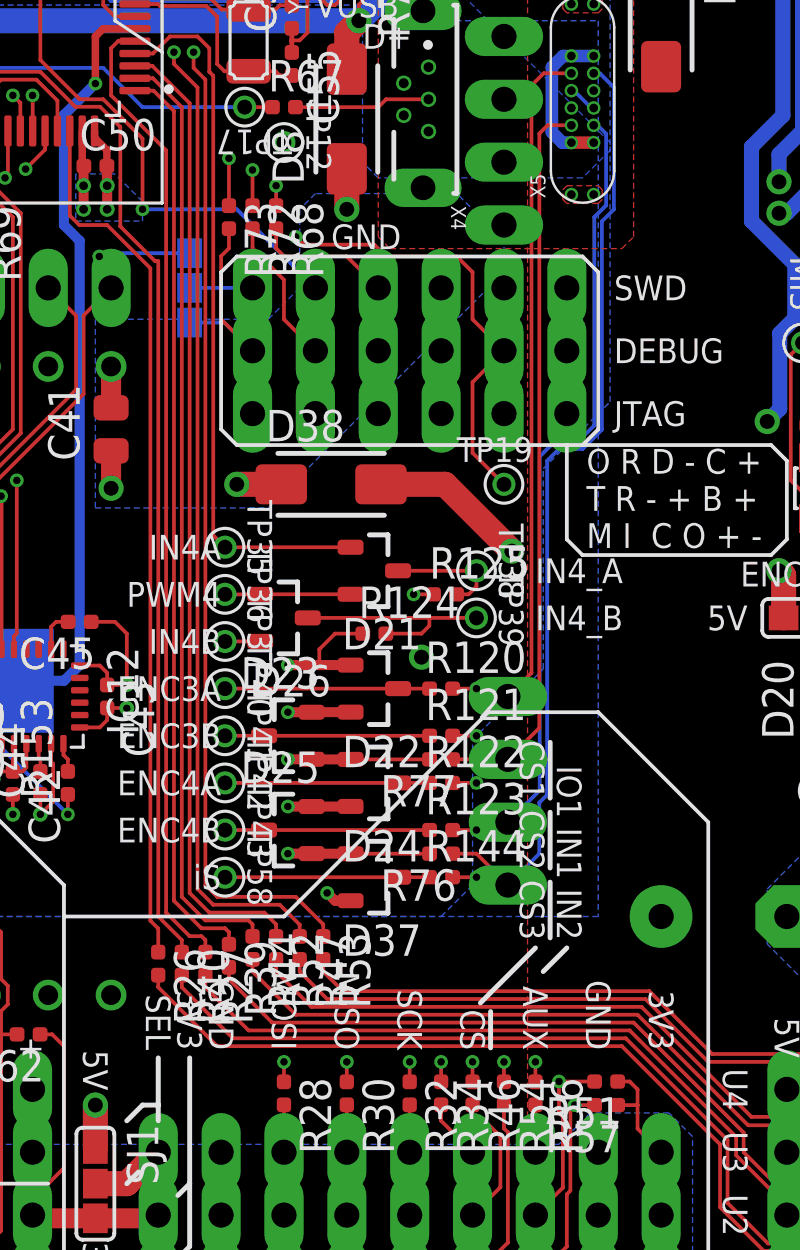
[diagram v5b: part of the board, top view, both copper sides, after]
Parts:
- moved R26 2.93 mm to (56.5, 14.0)
- moved R40 2.69 mm to (57.5, 14.0)
- moved R27 2.48 mm to (58.4, 14.0)
- moved R39 2.48 mm to (59.4, 14.3)
- moved R44 2.48 mm to (60.3, 14.6)
- moved R52 2.29 mm to (61.3, 14.6)
- moved R47 2.13 mm to (62.2, 14.6)
- moved R53 2.01 mm to (63.2, 14.6)
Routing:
- net UTS1_TRIG: track 38.3 -> 35.3 mm
- net UTS1-TRIG: track 32.0 -> 34.8 mm
- net UTS2_ECHO: track 46.6 -> 43.9 mm
- net UTS2-ECHO: track 33.8 -> 36.5 mm
- net UTS2_TRIG: track 39.6 -> 37.1 mm
- net UTS2-TRIG: track 27.4 -> 30.0 mm
- net UTS1-ECHO: track 38.6 -> 41.2 mm
- net UTS3_TRIG: track 40.7 -> 38.1 mm
- net UTS3-TRIG: track 25.1 -> 27.6 mm
- net UTS4-TRIG: track 24.1 -> 26.6 mm
- net UTS4_TRIG: track 41.7 -> 39.3 mm
- net UTS1_ECHO: track 41.8 -> 39.5 mm
- net UTS3_ECHO: track 62.7 -> 60.4 mm
- net UTS3-ECHO: track 27.1 -> 29.4 mm
- net UTS4-ECHO: track 24.1 -> 26.3 mm
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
